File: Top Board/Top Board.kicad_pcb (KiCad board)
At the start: 2 copper layers, 88.9 x 27.9 mm, 5 parts

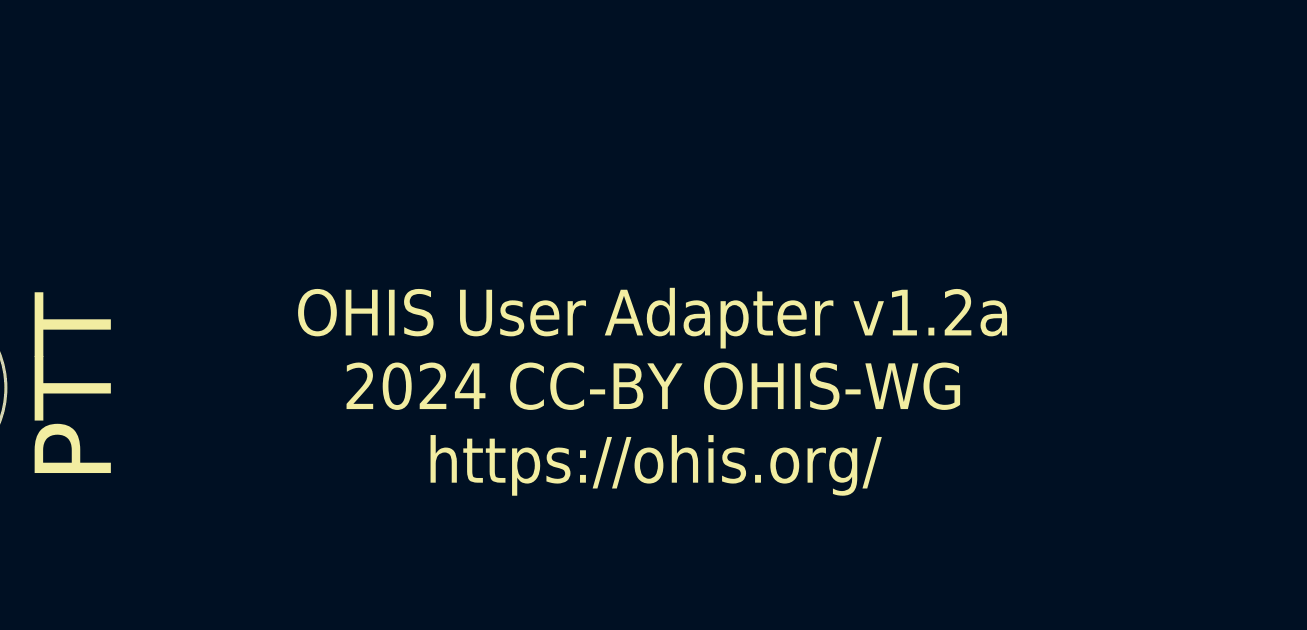
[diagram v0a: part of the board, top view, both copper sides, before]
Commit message: update top and bottom board silk screen to v1.3a
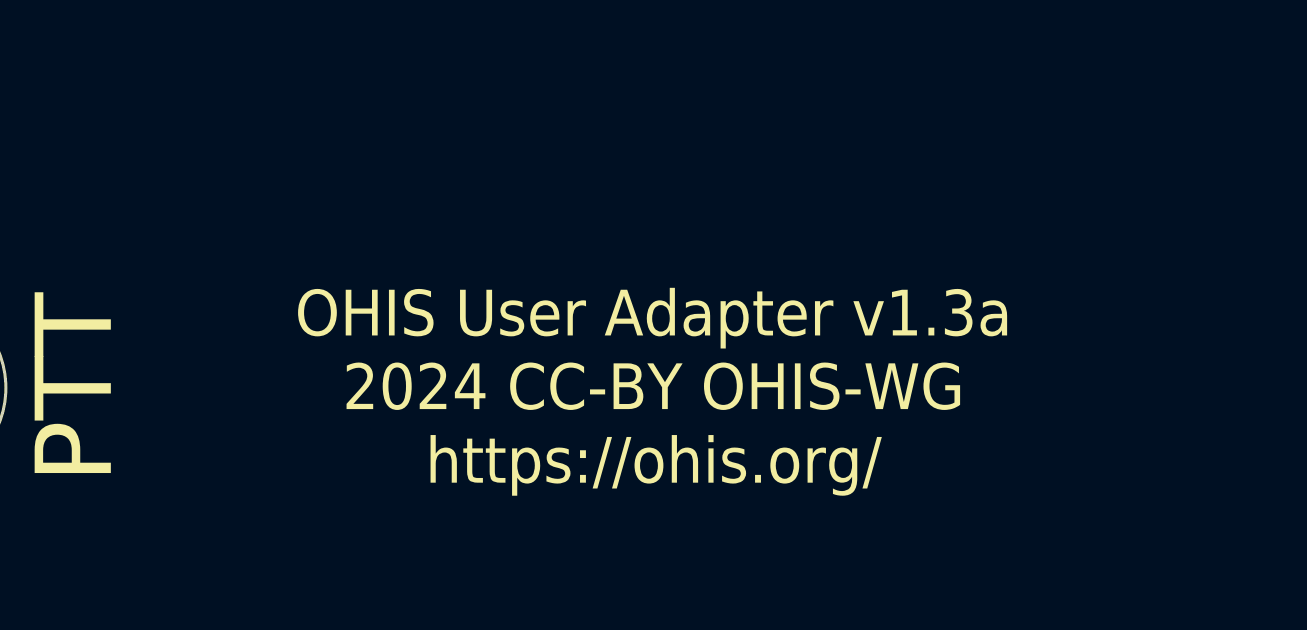
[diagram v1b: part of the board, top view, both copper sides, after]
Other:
- board text added: "OHIS User Adapter v1.3a 2024 CC-BY OHIS-WG https://ohis.org/"
- board text removed: "OHIS User Adapter v1.2a 2024 CC-BY OHIS-WG https://ohis.org/"
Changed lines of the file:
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@@
       (outputformat 1)
       (mirror false)
-      (drillshape 1)
+      (drillshape 0)
       (scaleselection 1)
-      (outputdirectory "")
+      (outputdirectory "C:/Users/derek.HOME/Desktop/user_adapter_v1.3a/top_board")
     )
   )
@@
     (effects (font (size 2.032 2.032) (thickness 0.254)) (justify bottom))
   )
-  (gr_text "OHIS User Adapter v1.2a\n2024 CC-BY OHIS-WG\nhttps://ohis.org/" (at 107.95 76.2) (layer "F.SilkS")
+  (gr_text "OHIS User Adapter v1.3a\n2024 CC-BY OHIS-WG\nhttps://ohis.org/" (at 107.95 76.2) (layer "F.SilkS")
     (effects (font (size 1.524 1.397) (thickness 0.2032)))
   )
